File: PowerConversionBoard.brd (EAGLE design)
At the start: 152.4 x 76.2 mm, 48 parts, among them U1 LM2678, U2 LM2678

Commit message: worked on board
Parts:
- moved J5 202.9 mm to (148.6, 72.4)
- moved J4 185.6 mm to (96.5, 71.1)
- moved R4 175.3 mm to (141.0, 61.0)
- moved U$13 167.0 mm to (142.2, 67.3)
- moved U$8 124.6 mm to (71.1, -6.35)
- moved U$14 105.2 mm to (63.5, -15.2)
- moved U$6 94.6 mm to (64.8, -6.35)
- moved J2 78.3 mm to (3.81, 66.0)
- moved J3 76.7 mm to (24.1, -5.08)
- moved U$11 71.6 mm to (54.6, -6.35)
- moved J1 63.3 mm to (3.81, 58.4)
- moved U$12 61.7 mm to (44.5, -6.35)
- moved R1 59.1 mm to (-11.4, 19.1)
- moved LED4 54.3 mm to (-11.4, 10.2)
- moved U$10 50.0 mm to (36.8, -6.35)
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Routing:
- net N$7: track 0.00 -> 44.4 mm
- net +5V_3.3V: track 0.00 -> 37.1 mm
- net GND: track 0.00 -> 18.2 mm

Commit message: updates
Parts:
- removed LED1, LED2, LED3, LED4: (no value), led:CHIP-LED0603
- added D1, D2, D3, D4: (no value), SparkFun-LED:LED-0603
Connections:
- new net N$4: D2.A, R5.1
- new net N$8: D1.A, R2.1
- net GND: now also D1.C, D2.C, D3.C, D4.C; no longer LED1.C, LED2.C, LED3.C, LED4.C
- net N$5: now also D3.A; no longer LED3.A
- net N$6: now also D4.A; no longer LED4.A
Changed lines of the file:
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@@
 <setting verticaltext="up"/>
 </settings>
-<grid distance="50" unitdist="mil" unit="inch" style="lines" multiple="1" display="no" altdistance="5" altunitdist="mil" altunit="inch"/>
+<grid distance="10" unitdist="mil" unit="mil" style="lines" multiple="1" display="yes" altdistance="5" altunitdist="mil" altunit="inch"/>
 <layers>
 <layer number="1" name="Top" color="4" fill="1" visible="yes" active="yes"/>
@@
 <attribute name="VALUE" x="-39.37" y="61.468" size="0.6096" layer="27" font="vector" ratio="20" align="top-center"/>
 </element>
-<element name="LED1" library="led" library_urn="urn:adsk.eagle:library:259" package="CHIP-LED0603" package3d_urn="urn:adsk.eagle:package:15819/3" value="" x="-59.69" y="55.88" smashed="yes">
-<attribute name="NAME" x="-60.325" y="55.245" size="1.27" layer="25" rot="R90"/>
-<attribute name="POPULARITY" value="26" x="0" y="0" size="1.778" layer="27" display="off"/>
-<attribute name="VALUE" x="-57.785" y="55.245" size="1.27" layer="27" rot="R90"/>
-</element>
-<element name="LED2" library="led" library_urn="urn:adsk.eagle:library:259" package="CHIP-LED0603" package3d_urn="urn:adsk.eagle:package:15819/3" value="" x="-63.5" y="55.88" smashed="yes">
-<attribute name="NAME" x="-64.135" y="55.245" size="1.27" layer="25" rot="R90"/>
-<attribute name="POPULARITY" value="26" x="0" y="0" size="1.778" layer="27" display="off"/>
-<attribute name="VALUE" x="-61.595" y="55.245" size="1.27" layer="27" rot="R90"/>
-</element>
-<element name="LED3" library="led" library_urn="urn:adsk.eagle:library:259" package="CHIP-LED0603" package3d_urn="urn:adsk.eagle:package:15819/3" value="" x="-7.62" y="68.58" smashed="yes">
-<attribute name="NAME" x="-8.255" y="67.945" size="1.27" layer="25" rot="R90"/>
-<attribute name="POPULARITY" value="26" x="6.35" y="6.35" size="1.778" layer="27" display="off"/>
-<attribute name="VALUE" x="-5.715" y="67.945" size="1.27" layer="27" rot="R90"/>
-</element>
 <element name="R2" library="SparkFun-Resistors" library_urn="urn:adsk.eagle:library:532" package="0603" package3d_urn="urn:adsk.eagle:package:39650/1" value="470" x="-46.99" y="62.23" smashed="yes">
 <attribute name="NAME" x="-46.99" y="62.992" size="0.6096" layer="25" font="vector" ratio="20" align="bottom-center"/>
@@
 <attribute name="PROD_ID" value="RES-07869" x="-11.43" y="25.4" size="1.778" layer="27" display="off"/>
 <attribute name="VALUE" x="-11.43" y="18.288" size="0.6096" layer="27" font="vector" ratio="20" align="top-center"/>
-</element>
-<element name="LED4" library="led" library_urn="urn:adsk.eagle:library:259" package="CHIP-LED0603" package3d_urn="urn:adsk.eagle:package:15819/3" value="" x="-11.43" y="10.16" smashed="yes">
-<attribute name="NAME" x="-12.065" y="9.525" size="1.27" layer="25" rot="R90"/>
-<attribute name="POPULARITY" value="26" x="-16.51" y="12.7" size="1.778" layer="27" display="off"/>
-<attribute name="VALUE" x="-9.525" y="9.525" size="1.27" layer="27" rot="R90"/>
 </element>
 <element name="C15" library="PowerComponents" package="CTAN(7.30_4.30MM)" value="10uF" x="12.7" y="41.91" smashed="yes" rot="R90"/>
@@
 </element>
 <element name="U$7" library="Conversion_Connector" package="CONVERSION_TSW_12X2" value="CONVERSION_TSW_12X2" x="148.59" y="22.86" smashed="yes" rot="R90"/>
+<element name="D1" library="SparkFun-LED" library_urn="urn:adsk.eagle:library:529" package="LED-0603" package3d_urn="urn:adsk.eagle:package:39354/1" value="" x="-63.5" y="-20.32" smashed="yes">
+<attribute name="NAME" x="-63.5" y="-19.685" size="0.6096" layer="25" font="vector" ratio="20" align="bottom-center"/>
+<attribute name="VALUE" x="-63.5" y="-20.955" size="0.6096" layer="27" font="vector" ratio="20" align="top-center"/>
+</element>
+<element name="D2" library="SparkFun-LED" library_urn="urn:adsk.eagle:library:529" package="LED-0603" package3d_urn="urn:adsk.eagle:package:39354/1" value="" x="-63.5" y="-24.13" smashed="yes">
+<attribute name="NAME" x="-63.5" y="-23.495" size="0.6096" layer="25" font="vector" ratio="20" align="bottom-center"/>
+<attribute name="VALUE" x="-63.5" y="-24.765" size="0.6096" layer="27" font="vector" ratio="20" align="top-center"/>
+</element>
+<element name="D3" library="SparkFun-LED" library_urn="urn:adsk.eagle:library:529" package="LED-0603" package3d_urn="urn:adsk.eagle:package:39354/1" value="" x="-63.5" y="-27.94" smashed="yes">
+<attribute name="NAME" x="-63.5" y="-27.305" size="0.6096" layer="25" font="vector" ratio="20" align="bottom-center"/>
+<attribute name="VALUE" x="-63.5" y="-28.575" size="0.6096" layer="27" font="vector" ratio="20" align="top-center"/>
+</element>
+<element name="D4" library="SparkFun-LED" library_urn="urn:adsk.eagle:library:529" package="LED-0603" package3d_urn="urn:adsk.eagle:package:39354/1" value="" x="-63.5" y="-31.75" smashed="yes">
+<attribute name="NAME" x="-63.5" y="-31.115" size="0.6096" layer="25" font="vector" ratio="20" align="bottom-center"/>
+<attribute name="VALUE" x="-63.5" y="-32.385" size="0.6096" layer="27" font="vector" ratio="20" align="top-center"/>
+</element>
 </elements>
 <signals>
@@
 <contactref element="C11" pad="-"/>
 <contactref element="C12" pad="-"/>
-<contactref element="LED2" pad="C"/>
-<contactref element="LED1" pad="C"/>
-<contactref element="LED3" pad="C"/>
-<contactref element="LED4" pad="C"/>
 <contactref element="J2" pad="P$1"/>
 <contactref element="U$11" pad="P$1"/>
@@
 <wire x1="73.66" y1="55.2" x2="68.735" y2="55.2" width="0.1524" layer="1"/>
 <wire x1="68.735" y1="55.2" x2="68.325" y2="55.61" width="0.1524" layer="1"/>
+<contactref element="D3" pad="C"/>
+<contactref element="D4" pad="C"/>
+<contactref element="D1" pad="C"/>
+<contactref element="D2" pad="C"/>
 <wire x1="130.81" y1="59.15" x2="140.12" y2="60.96" width="0" layer="19" extent="1-1"/>
 <wire x1="130.81" y1="69.75" x2="130.81" y2="59.15" width="0" layer="19" extent="1-1"/>
@@
 <wire x1="12.7" y1="65.36" x2="19.05" y2="65.36" width="0" layer="19" extent="1-1"/>
 <wire x1="3.81" y1="66.04" x2="12.7" y2="65.36" width="0" layer="19" extent="1-1"/>
-<wire x1="-7.62" y1="69.33" x2="3.81" y2="66.04" width="0" layer="19" extent="1-1"/>
-<wire x1="-11.43" y1="10.91" x2="12.7" y2="45.13" width="0" layer="19" extent="1-1"/>
-<wire x1="24.13" y1="-5.08" x2="-11.43" y2="10.91" width="0" layer="19" extent="1-1"/>
+<wire x1="24.13" y1="-5.08" x2="36.83" y2="41.49" width="0" layer="19" extent="1-1"/>
 <wire x1="54.61" y1="-6.35" x2="24.13" y2="-5.08" width="0" layer="19" extent="1-1"/>
-<wire x1="-59.69" y1="56.63" x2="-7.62" y2="69.33" width="0" layer="19" extent="1-1"/>
-<wire x1="-63.5" y1="56.63" x2="-59.69" y2="56.63" width="0" layer="19" extent="1-1"/>
+<wire x1="-62.623" y1="-20.32" x2="24.13" y2="-5.08" width="0" layer="19" extent="1-1"/>
+<wire x1="-62.623" y1="-24.13" x2="-62.623" y2="-20.32" width="0" layer="19" extent="1-1"/>
+<wire x1="-62.623" y1="-27.94" x2="-62.623" y2="-24.13" width="0" layer="19" extent="1-1"/>
+<wire x1="-62.623" y1="-31.75" x2="-62.623" y2="-27.94" width="0" layer="19" extent="1-1"/>
 </signal>
 <signal name="+5V">
@@
 <wire x1="-38.52" y1="62.23" x2="40.64" y2="41.1988" width="0" layer="19" extent="1-1"/>
 </signal>
-<signal name="N$5">
-<contactref element="LED3" pad="A"/>
-<contactref element="R3" pad="1"/>
-<wire x1="-51.65" y1="62.23" x2="-7.62" y2="67.83" width="0" layer="19" extent="1-1"/>
-</signal>
-<signal name="N$6">
-<contactref element="LED4" pad="A"/>
-<contactref element="R1" pad="1"/>
-<wire x1="-11.43" y1="9.41" x2="-12.28" y2="19.05" width="0" layer="19" extent="1-1"/>
-</signal>
 <signal name="N$20">
 <contactref element="U1" pad="2"/>
@@
 <wire x1="12.7" y1="38.69" x2="19.05" y2="38.69" width="0" layer="19" extent="1-1"/>
 </signal>
+<signal name="N$4">
+<contactref element="D2" pad="A"/>
+<contactref element="R5" pad="1"/>
+<wire x1="-55.46" y1="62.23" x2="-64.377" y2="-24.13" width="0" layer="19" extent="1-1"/>
+</signal>
+<signal name="N$5">
+<contactref element="D3" pad="A"/>
+<contactref element="R3" pad="1"/>
+<wire x1="-51.65" y1="62.23" x2="-64.377" y2="-27.94" width="0" layer="19" extent="1-1"/>
+</signal>
+<signal name="N$6">
+<contactref element="D4" pad="A"/>
+<contactref element="R1" pad="1"/>
+<wire x1="-12.28" y1="19.05" x2="-64.377" y2="-31.75" width="0" layer="19" extent="1-1"/>
+</signal>
+<signal name="N$8">
+<contactref element="R2" pad="1"/>
+<contactref element="D1" pad="A"/>
+<wire x1="-47.84" y1="62.23" x2="-64.377" y2="-20.32" width="0" layer="19" extent="1-1"/>
+</signal>
 </signals>

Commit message: updated board
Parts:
- removed U$7: CONVERSION_TSW_12X2, Conversion_Connector:CONVERSION_TSW_12X2
- added U$9: CONVERSION_TSW_12X2, Dist_to_Conversion_Connector:CONVERSION_TSW_12X2
- moved J3 124.6 mm to (147.2, 14.3)
- moved D4 108.9 mm to (35.8, 13.0), turned to 90 degrees
- moved D3 103.9 mm to (32.0, 13.0), turned to 90 degrees
- moved D2 98.9 mm to (28.2, 13.0), turned to 90 degrees
- moved D1 94.0 mm to (24.4, 13.0), turned to 90 degrees
- moved C20 84.7 mm to (31.4, 22.0)
- moved C6 84.7 mm to (35.2, 22.0)
- moved R2 84.7 mm to (27.6, 22.0)
- moved R5 84.7 mm to (19.9, 22.0)
- moved R3 84.7 mm to (23.7, 22.0)
- moved R1 57.6 mm to (46.0, 15.2)
- moved U$10 31.1 mm to (57.0, 17.4)
- moved U$11 31.1 mm to (74.8, 17.4)
- moved U$12 31.1 mm to (64.6, 17.4)
- moved U$14 31.1 mm to (83.6, 8.51)
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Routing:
- net GND: track 18.2 -> 70.0 mm
- net +12V: track 0.00 -> 25.1 mm
- net N$20: track 0.00 -> 19.1 mm
- net N$7: track 44.4 -> 42.6 mm
- net +5V_3.3V: track 37.1 -> 36.4 mm

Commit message: Did some stuff
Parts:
- removed U$12, U$14: TP, TP:TP
- added U$7: HCM1305, HCM1305:HCM1305
- U$5: value HCM1305 -> TP; device HCM1305:HCM1305 -> TP:TP
- moved J6 129.2 mm to (147.2, 15.1)
- moved R3 126.2 mm to (143.7, 61.3), turned to 90 degrees
- moved D3 124.7 mm to (147.3, 60.4), turned to 0 degrees
- moved D1 123.2 mm to (147.3, 4.93), turned to 180 degrees
- moved R2 121.4 mm to (147.4, 2.74), turned to 180 degrees
- moved D4 91.2 mm to (106.6, 70.5), turned to 270 degrees
- moved R1 84.5 mm to (107.7, 72.9), turned to 180 degrees
- moved U$6 78.3 mm to (147.4, 64.5)
- moved U$5 74.3 mm to (4.93, 71.7)
- moved U$11 73.0 mm to (147.2, 8.56)
- moved D2 61.8 mm to (8.33, 71.6), turned to 270 degrees
- moved U$10 59.8 mm to (11.6, 56.3), turned to 270 degrees
- moved U$8 54.9 mm to (103.0, 71.0)
- moved R5 50.5 mm to (10.3, 71.6), turned to 270 degrees
- moved C20 46.0 mm to (56.6, 60.5), turned to 90 degrees
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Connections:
- net +12V: now also U$5.P$1; no longer U$12.P$1, U$14.P$1
- net +5V: now also U$11.P$1, U$2.2; no longer U$10.P$1, U$5.2
- net +5V_3.3V: now also U$7.2; no longer U$2.2
- net GND: now also U$10.P$1; no longer U$11.P$1
- net N$1: now also U$2.1; no longer U$5.1
- net N$7: now also U$7.1; no longer U$2.1
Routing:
- net GND: track 70.0 -> 335.6 mm, vias 0 -> 2
- net +5V: track 0.00 -> 135.5 mm
- net +12V: track 25.1 -> 73.9 mm
- net +5V_3.3V: track 36.4 -> 74.7 mm
- net N$1: track 0.00 -> 33.8 mm
- net N$20: track 19.1 -> 43.0 mm
- net +3.3V: track 0.00 -> 10.9 mm
- net N$2: track 0.00 -> 9.30 mm, vias 0 -> 2
- net N$3: track 0.00 -> 7.44 mm, vias 0 -> 1
- net N$7: track 42.6 -> 38.7 mm
- net N$6: track 0.00 -> 3.05 mm
- net N$5: track 0.00 -> 2.83 mm
- net N$8: track 0.00 -> 2.19 mm
- net N$4: track 0.00 -> 1.93 mm

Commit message: done
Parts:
- moved U$4 5.84 mm to (122.6, 67.9)
- moved U$13 5.80 mm to (136.8, 62.6), turned to 270 degrees
- moved R4 5.46 mm to (136.8, 57.5), turned to 90 degrees
- moved U$7 5.05 mm to (77.7, 66.1)
- moved C24 4.16 mm to (77.7, 55.0)
- moved C26 4.16 mm to (84.0, 55.0)
- moved C25 4.16 mm to (71.3, 55.0)
- moved C14 3.53 mm to (32.0, 65.2)
- moved C29 3.53 mm to (38.2, 65.3)
- moved C3 3.53 mm to (43.0, 65.5)
- moved C30 3.53 mm to (25.8, 65.2)
- moved U2 3.53 mm to (50.9, 66.3)
- moved C20 3.53 mm to (57.0, 57.0)
- moved U$3 3.53 mm to (62.8, 55.9)
- moved C31 3.53 mm to (19.5, 65.3)
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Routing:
- net GND: track 335.6 -> 427.1 mm, vias 2 -> 6
- net +5V_3.3V: track 74.7 -> 105.4 mm, vias 0 -> 2
- net +3.3V: track 10.9 -> 40.9 mm
- net N$10: track 0.00 -> 3.51 mm
- net +5V: track 135.5 -> 132.4 mm
- net N$7: track 38.7 -> 37.0 mm
- net N$3: track 7.44 -> 9.04 mm, vias 1 -> 2
- net +12V: track 73.9 -> 72.9 mm

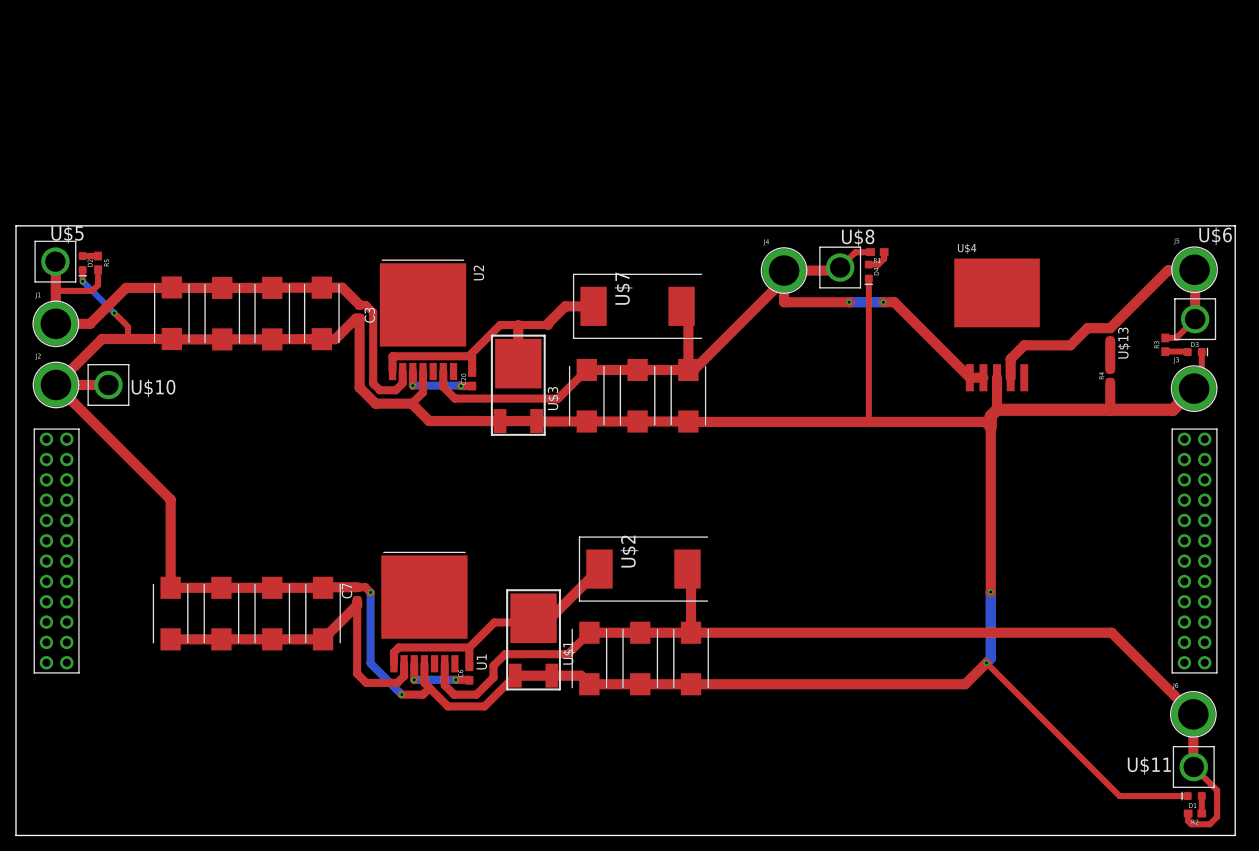
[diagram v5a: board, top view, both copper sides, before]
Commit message: added connector for backplane
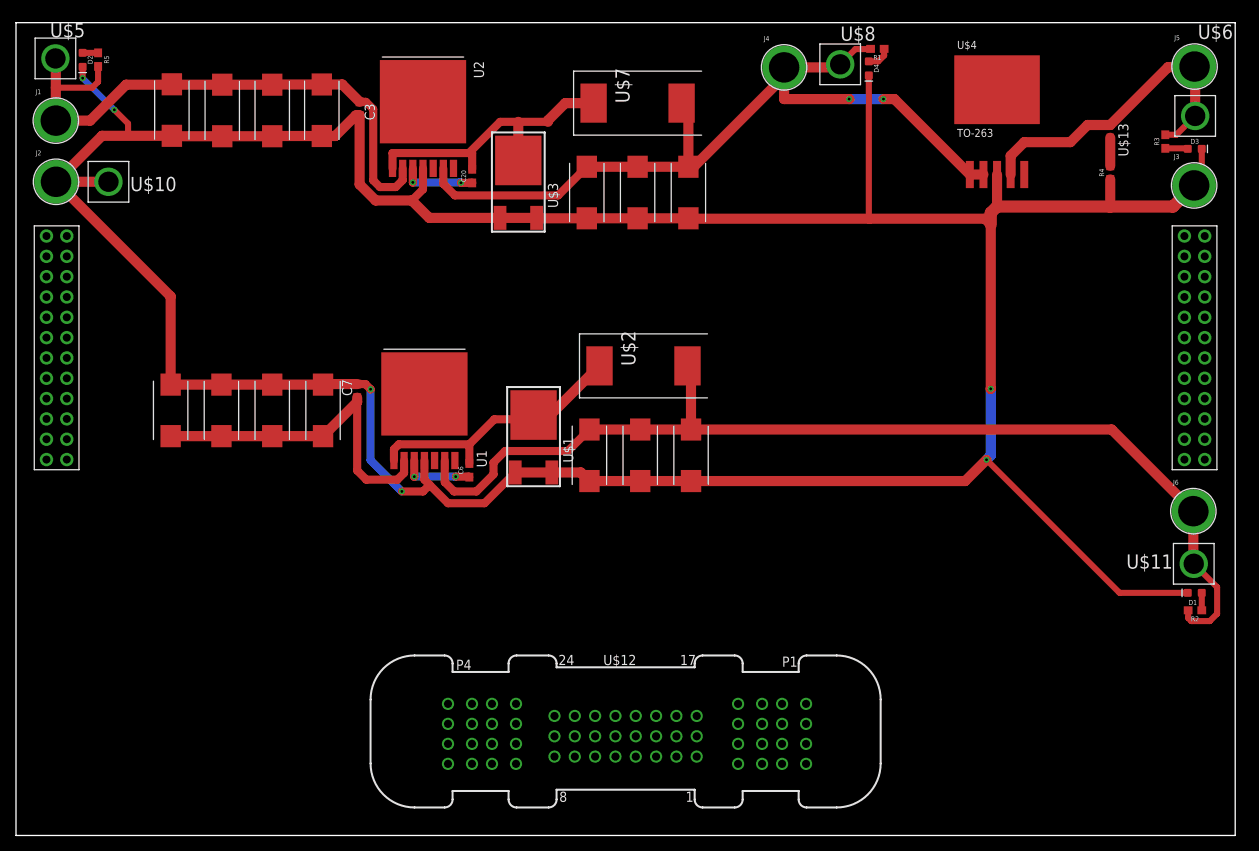
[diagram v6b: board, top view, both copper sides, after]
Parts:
- added U$12: ET60S-02-24-02-X-VP-GP, ET60S-02-24-02-X-VP-GP:ET60S-02-24-02-X-VP-GP
- moved C14 25.4 mm to (32.0, 90.6)
- moved C29 25.4 mm to (38.2, 90.7)
- moved C3 25.4 mm to (43.0, 90.9)
- moved C30 25.4 mm to (25.8, 90.6)
- moved D2 25.4 mm to (8.33, 97.0)
- moved D4 25.4 mm to (106.6, 95.9)
- moved J1 25.4 mm to (4.98, 89.4)
- moved J4 25.4 mm to (96.0, 96.0)
- moved J5 25.4 mm to (147.3, 96.1)
- moved R1 25.4 mm to (107.7, 98.3)
- moved U$6 25.4 mm to (147.4, 89.9)
- moved U$7 25.4 mm to (77.7, 91.5)
- moved U$8 25.4 mm to (103.0, 96.4)
- moved U$9 25.4 mm to (3.81, 74.9)
- moved C10 25.4 mm to (78.0, 47.5)
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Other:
- board size 152.4 x 76.2 mm -> 152.4 x 101.6 mm
